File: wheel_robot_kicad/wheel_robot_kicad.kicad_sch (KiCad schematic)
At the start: 7 parts, among them M1 Motor_DC, M2 Motor_DC, U1 ESP32-C6-MINI-1, U2 LM2596S-3.3, U3 BMI160, U4 DRV8833PW, U5 DRV8833PW

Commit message: added additional IMU documentation
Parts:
- removed U1: ESP32-C6-MINI-1, RF_Module:ESP32-C6-MINI-1, symbol RF_Module:ESP32-C6-MINI-1
- removed U2: LM2596S-3.3, Package_TO_SOT_SMD:TO-263-5_TabPin3, symbol Regulator_Switching:LM2596S-3.3
- removed U4, U5: DRV8833PW, Package_SO:TSSOP-16_4.4x5mm_P0.65mm, symbol Driver_Motor:DRV8833PW
- added 450mAh_3S_LiPo_BatteryPack_45C: 11.1V, symbol Device:Battery_Cell
- added D1: 1N5822, Diode_THT:D_DO-201AD_P15.24mm_Horizontal, symbol Diode:1N5822
- added L1: 68uH, symbol Device:L
- added U1: ESP32-S3-DEVKITC-1-N8R8, ESP32-S3-DEVKITC-1-N8R8:ESP32-S3-DEVKITC-1-N8R8, symbol ESP32-S3-DEVKITC-1-N8R8:ESP32-S3-DEVKITC-1-N8R8
- added U2: TB6612FNG, Package_SO:SSOP-24_5.3x8.2mm_P0.65mm, symbol Driver_Motor:TB6612FNG
- added U4: LM2596S-5, Package_TO_SOT_SMD:TO-263-5_TabPin3, symbol Regulator_Switching:LM2596S-5
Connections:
- net GND: now also 450mAh_3S_LiPo_BatteryPack_45C.2 (-), D1.2 (A), U1.J1_22 (GND3), U1.J3_1 (GND), U1.J3_10 (GPIO38), U1.J3_11 (GPIO37), U1.J3_12 (GPIO36), U1.J3_13 (GPIO35), U1.J3_14 (GPIO0), U1.J3_15 (GPIO45), U1.J3_16 (GPIO48), U1.J3_17 (GPIO47), U1.J3_18 (GPIO21), U1.J3_19 (USB_D+/GPIO20), U1.J3_2 (U0TXD/GPIO43), U1.J3_20 (USB_D-/GPIO19), U1.J3_21 (GND1), U1.J3_22 (GND2), U1.J3_3 (U0RXD/GPIO44), U1.J3_4 (GPIO1), U1.J3_5 (GPIO2), U1.J3_6 (MTMS/GPIO42), U1.J3_7 (MTDI/GPIO41), U1.J3_8 (MTDO/GPIO40), U1.J3_9 (MTCK/GPIO39), U2.10 (PGND2), U2.16 (BIN2), U2.17 (BIN1), U2.18 (GND), U2.21 (AIN1), U2.22 (AIN2), U2.3 (PGND1), U2.4 (PGND1), U2.9 (PGND2), U4.3 (GND), U4.5 (~{ON}/OFF); no longer U3.7 (GND)
- net at U3.5 (VDDIO): no longer U3.8 (VDD)
- net at M1.1 (+): now also U2.7 (BO2), U2.8 (BO2)
- net at M1.2 (-): now also U2.11 (BO1), U2.12 (BO1)
- net at M2.1 (+): now also U2.1 (AO1), U2.2 (AO1)
- net at M2.2 (-): now also U2.5 (AO2), U2.6 (AO2)
- new net: D1.1 (K), L1.1, U4.2 (OUT)
- new net: 450mAh_3S_LiPo_BatteryPack_45C.1 (+), U4.1 (VIN)
- new net: U1.J1_18 (GPIO12), U2.15 (PWMB)
- new net: U1.J1_19 (GPIO13), U2.23 (PWMA)
- new net: U1.J1_20 (GPIO14), U2.19 (STBY)
- new net: L1.2, U1.J1_21 (5V0), U2.20 (VCC), U4.4 (FB)
- new net: U2.13 (VM2), U2.14 (VM3), U2.24 (VM1)

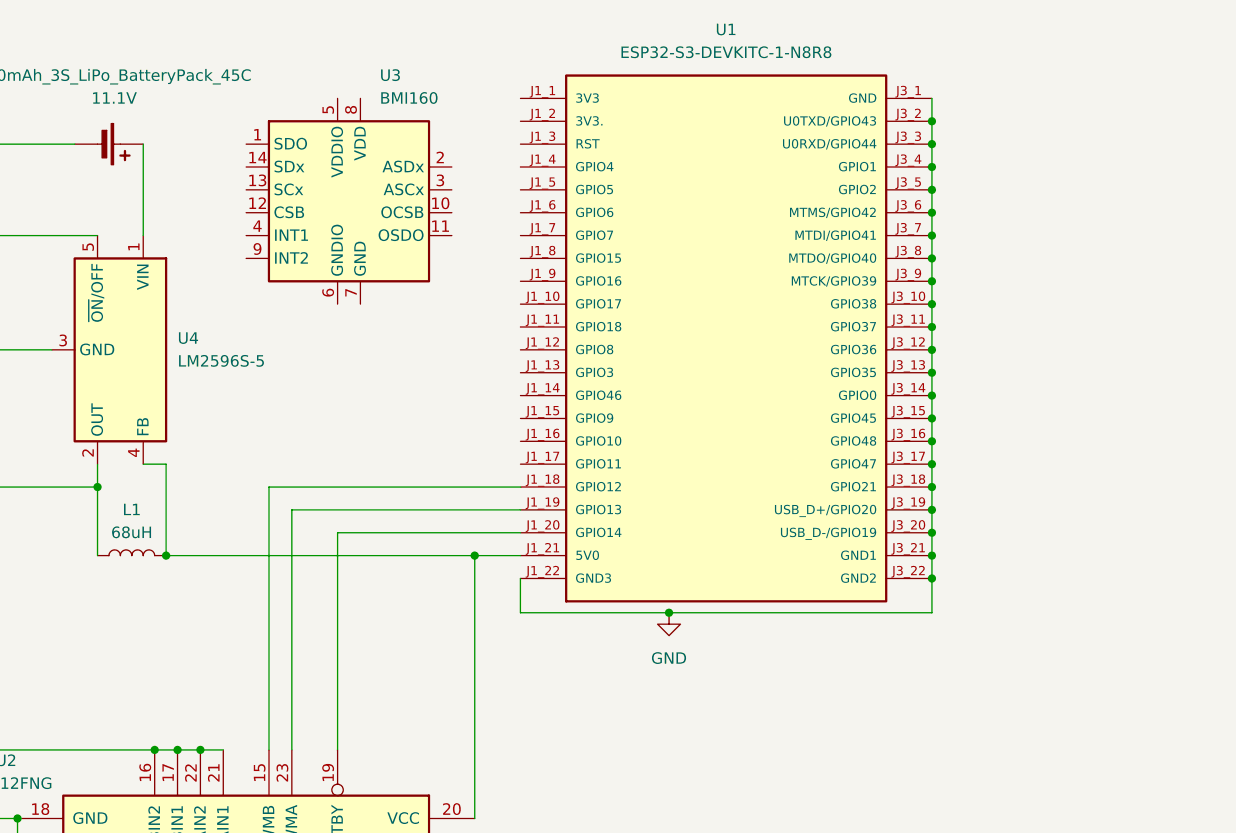
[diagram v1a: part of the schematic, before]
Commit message: updated current design to include ordered footprints
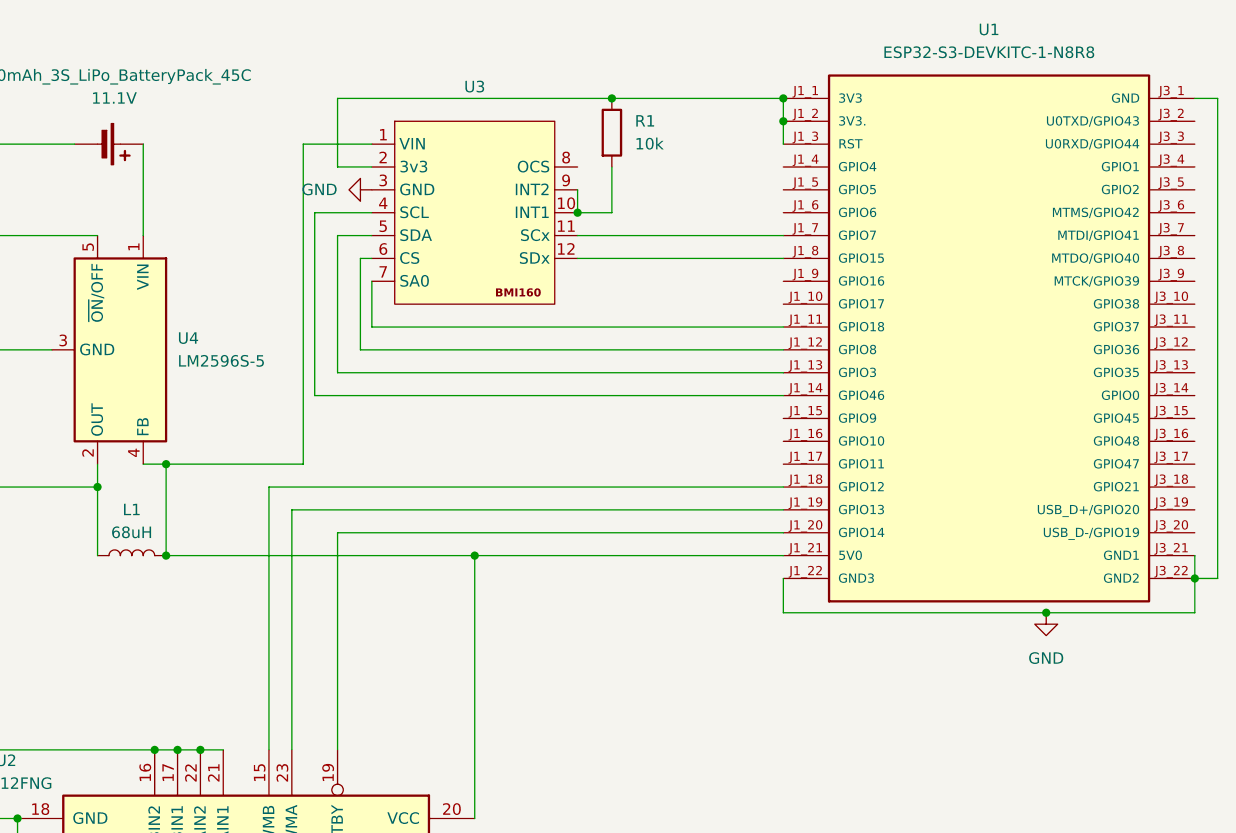
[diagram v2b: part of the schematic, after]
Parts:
- removed U3: BMI160, Package_LGA:Bosch_LGA-14_3x2.5mm_P0.5mm, symbol Sensor_Motion:BMI160
- added R1: 10k, symbol Device:R
- added U3: ~, KappyCustom:BMI160_Module_SMD, symbol KappyCustom:BMI160_Module
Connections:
- net GND: now also U3.3 (GND); no longer U1.J3_10 (GPIO38), U1.J3_11 (GPIO37), U1.J3_12 (GPIO36), U1.J3_13 (GPIO35), U1.J3_14 (GPIO0), U1.J3_15 (GPIO45), U1.J3_16 (GPIO48), U1.J3_17 (GPIO47), U1.J3_18 (GPIO21), U1.J3_19 (USB_D+/GPIO20), U1.J3_2 (U0TXD/GPIO43), U1.J3_20 (USB_D-/GPIO19), U1.J3_3 (U0RXD/GPIO44), U1.J3_4 (GPIO1), U1.J3_5 (GPIO2), U1.J3_6 (MTMS/GPIO42), U1.J3_7 (MTDI/GPIO41), U1.J3_8 (MTDO/GPIO40), U1.J3_9 (MTCK/GPIO39)
- net at U1.J1_1 (3V3): now also U1.J1_2 (3V3.), U1.J1_3 (RST), R1.1, U3.2 (3v3)
- net at U1.J1_11 (GPIO18): now also U3.7 (SA0)
- net at U1.J1_12 (GPIO8): now also U3.6 (CS)
- net at U1.J1_13 (GPIO3): now also U3.5 (SDA)
- net at U1.J1_14 (GPIO46): now also U3.4 (SCL)
- net at L1.2, U1.J1_21 (5V0), U2.20 (VCC)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: now also U3.1 (VIN)
- net at U1.J1_7 (GPIO7): now also U3.11 (SCx)
- net at U1.J1_8 (GPIO15): now also U3.12 (SDx)
- new net: R1.2, U3.10 (INT1), U3.9 (INT2)
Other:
- moved on the sheet: U1

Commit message: added motor power
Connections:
- net at 450mAh_3S_LiPo_BatteryPack_45C.1 (+), U4.1 (VIN): now also U2.13 (VM2), U2.14 (VM3), U2.24 (VM1)
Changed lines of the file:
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@@
+	)
+	(junction
+		(at 48.26 30.48)
+		(diameter 0)
+		(color 0 0 0 0)
+	)
+	(junction
+		(at 85.09 118.11)
+		(diameter 0)
+		(color 0 0 0 0)
 	)
 	(junction
@@
 	)
 	(junction
-		(at 85.09 118.11)
-		(diameter 0)
-		(color 0 0 0 0)
-	)
-	(junction
 		(at 49.53 97.79)
 		(diameter 0)
@@
 	(wire
 		(pts
+			(xy 85.09 118.11) (xy 177.8 118.11)
+		)
+		(stroke
+			(width 0)
+			(type default)
+		)
+	)
+	(wire
+		(pts
 			(xy 66.04 66.04) (xy 50.8 66.04)
 		)
@@
 	(wire
 		(pts
+			(xy 69.85 139.7) (xy 76.2 139.7)
+		)
+		(stroke
+			(width 0)
+			(type default)
+		)
+	)
+	(wire
+		(pts
+			(xy 73.66 40.64) (xy 69.85 40.64)
+		)
+		(stroke
+			(width 0)
+			(type default)
+		)
+	)
+	(wire
+		(pts
+			(xy 72.39 43.18) (xy 72.39 53.34)
+		)
+		(stroke
+			(width 0)
+			(type default)
+		)
+	)
+	(wire
+		(pts
+			(xy 43.18 68.58) (xy 43.18 76.2)
+		)
+		(stroke
+			(width 0)
+			(type default)
+		)
+	)
+	(wire
+		(pts
+			(xy 34.29 105.41) (xy 34.29 115.57)
+		)
+		(stroke
+			(width 0)
+			(type default)
+		)
+	)
+	(wire
+		(pts
+			(xy 64.77 128.27) (xy 64.77 139.7)
+		)
+		(stroke
+			(width 0)
+			(type default)
+		)
+	)
+	(wire
+		(pts
+			(xy 167.64 78.74) (xy 165.1 78.74)
+		)
+		(stroke
+			(width 0)
+			(type default)
+		)
+	)
+	(wire
+		(pts
+			(xy 60.96 139.7) (xy 60.96 149.86)
+		)
+		(stroke
+			(width 0)
+			(type default)
+		)
+	)
+	(wire
+		(pts
+			(xy 119.38 76.2) (xy 85.09 76.2)
+		)
+		(stroke
+			(width 0)
+			(type default)
+		)
+	)
+	(wire
+		(pts
+			(xy 96.52 35.56) (xy 96.52 38.1)
+		)
+		(stroke
+			(width 0)
+			(type default)
+		)
+	)
+	(wire
+		(pts
+			(xy 148.59 82.55) (xy 165.1 82.55)
+		)
+		(stroke
+			(width 0)
+			(type default)
+		)
+	)
+	(wire
+		(pts
+			(xy 50.8 66.04) (xy 48.26 66.04)
+		)
+		(stroke
+			(width 0)
+			(type default)
+		)
+	)
+	(wire
+		(pts
+			(xy 69.85 73.66) (xy 119.38 73.66)
+		)
+		(stroke
+			(width 0)
+			(type default)
+		)
+	)
+	(wire
+		(pts
 			(xy 85.09 118.11) (xy 85.09 120.65)
 		)
@@
 	(wire
 		(pts
-			(xy 69.85 139.7) (xy 76.2 139.7)
-		)
-		(stroke
-			(width 0)
-			(type default)
-		)
-	)
-	(wire
-		(pts
-			(xy 73.66 40.64) (xy 69.85 40.64)
-		)
-		(stroke
-			(width 0)
-			(type default)
-		)
-	)
-	(wire
-		(pts
-			(xy 72.39 43.18) (xy 72.39 53.34)
-		)
-		(stroke
-			(width 0)
-			(type default)
-		)
-	)
-	(wire
-		(pts
-			(xy 43.18 68.58) (xy 43.18 76.2)
-		)
-		(stroke
-			(width 0)
-			(type default)
-		)
-	)
-	(wire
-		(pts
-			(xy 34.29 105.41) (xy 34.29 115.57)
-		)
-		(stroke
-			(width 0)
-			(type default)
-		)
-	)
-	(wire
-		(pts
-			(xy 64.77 128.27) (xy 64.77 139.7)
-		)
-		(stroke
-			(width 0)
-			(type default)
-		)
-	)
-	(wire
-		(pts
-			(xy 167.64 78.74) (xy 165.1 78.74)
-		)
-		(stroke
-			(width 0)
-			(type default)
-		)
-	)
-	(wire
-		(pts
-			(xy 60.96 139.7) (xy 60.96 149.86)
-		)
-		(stroke
-			(width 0)
-			(type default)
-		)
-	)
-	(wire
-		(pts
-			(xy 119.38 76.2) (xy 85.09 76.2)
-		)
-		(stroke
-			(width 0)
-			(type default)
-		)
-	)
-	(wire
-		(pts
-			(xy 96.52 35.56) (xy 96.52 38.1)
-		)
-		(stroke
-			(width 0)
-			(type default)
-		)
-	)
-	(wire
-		(pts
-			(xy 148.59 82.55) (xy 165.1 82.55)
-		)
-		(stroke
-			(width 0)
-			(type default)
-		)
-	)
-	(wire
-		(pts
-			(xy 50.8 66.04) (xy 48.26 66.04)
-		)
-		(stroke
-			(width 0)
-			(type default)
-		)
-	)
-	(wire
-		(pts
-			(xy 69.85 73.66) (xy 119.38 73.66)
-		)
-		(stroke
-			(width 0)
-			(type default)
-		)
-	)
-	(wire
-		(pts
 			(xy 165.1 78.74) (xy 165.1 76.2)
 		)
@@
 	(wire
 		(pts
+			(xy 177.8 13.97) (xy 64.77 13.97)
+		)
+		(stroke
+			(width 0)
+			(type default)
+		)
+	)
+	(wire
+		(pts
 			(xy 21.59 30.48) (xy 21.59 40.64)
 		)
@@
 	(wire
 		(pts
+			(xy 177.8 118.11) (xy 177.8 13.97)
+		)
+		(stroke
+			(width 0)
+			(type default)
+		)
+	)
+	(wire
+		(pts
 			(xy 66.04 30.48) (xy 66.04 66.04)
 		)
@@
 	(wire
 		(pts
+			(xy 85.09 115.57) (xy 85.09 118.11)
+		)
+		(stroke
+			(width 0)
+			(type default)
+		)
+	)
+	(wire
+		(pts
 			(xy 69.85 97.79) (xy 69.85 73.66)
 		)
@@
 	(wire
 		(pts
+			(xy 64.77 13.97) (xy 64.77 30.48)
+		)
+		(stroke
+			(width 0)
+			(type default)
+		)
+	)
+	(wire
+		(pts
 			(xy 52.07 97.79) (xy 49.53 97.79)
 		)
@@
 	(wire
 		(pts
+			(xy 64.77 30.48) (xy 48.26 30.48)
+		)
+		(stroke
+			(width 0)
+			(type default)
+		)
+	)
+	(wire
+		(pts
 			(xy 34.29 115.57) (xy 34.29 120.65)
 		)
@@
 		)
 		(stroke
-			(width 0)
-			(type default)
-		)
-	)
-	(wire
-		(pts
-			(xy 85.09 115.57) (xy 85.09 118.11)
-		)
-		(stroke

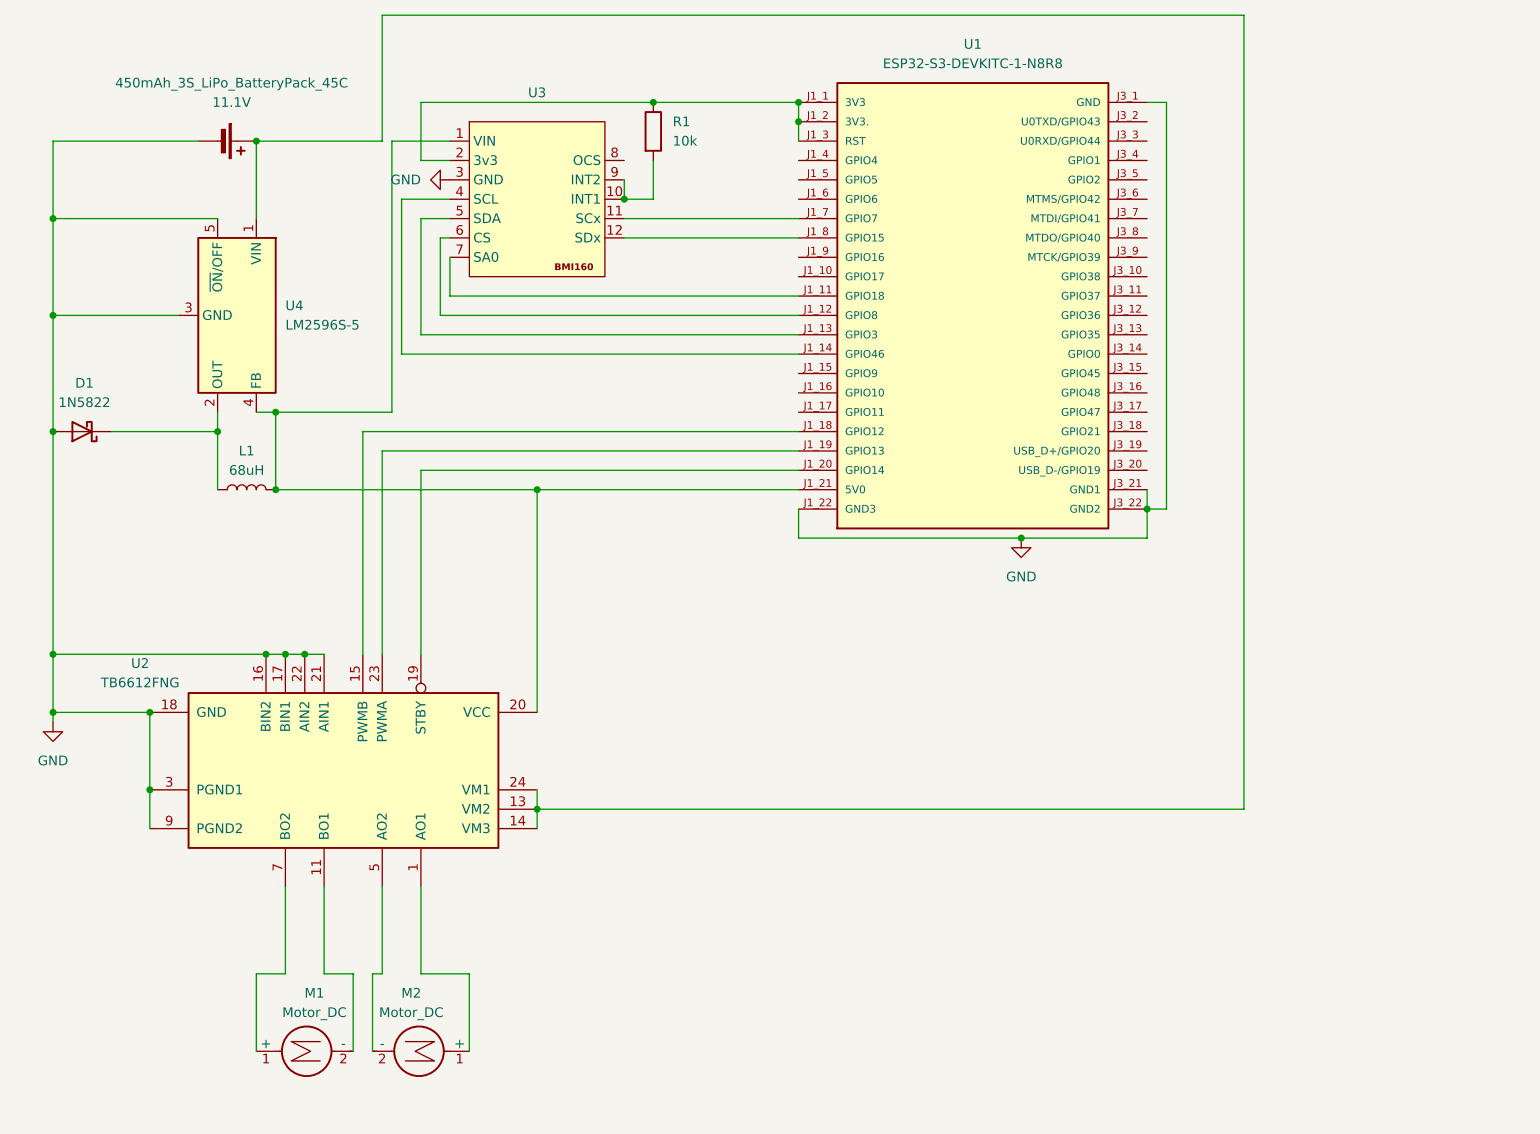
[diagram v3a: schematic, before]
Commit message: updated the curcuit to the current assembly state
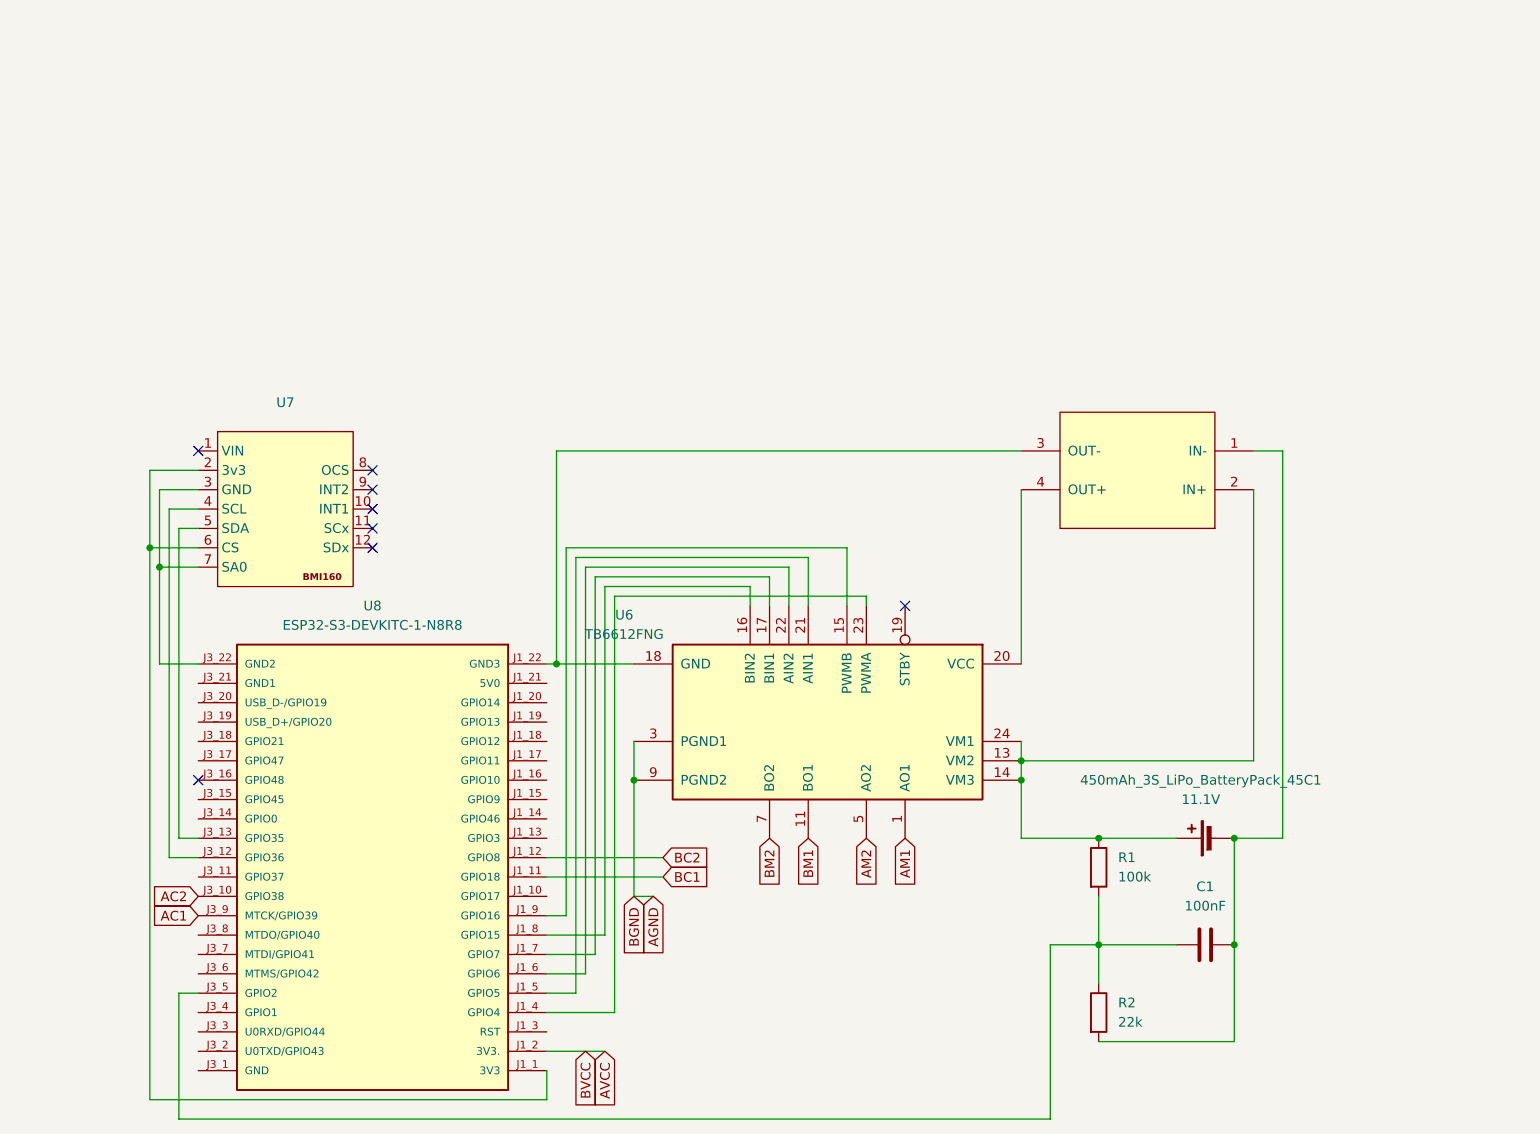
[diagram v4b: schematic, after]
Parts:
- removed 450mAh_3S_LiPo_BatteryPack_45C: 11.1V, symbol Device:Battery_Cell
- removed D1: 1N5822, Diode_THT:D_DO-201AD_P15.24mm_Horizontal, symbol Diode:1N5822
- removed L1: 68uH, symbol Device:L
- removed M1, M2: Motor_DC, symbol Motor:Motor_DC
- removed U1: ESP32-S3-DEVKITC-1-N8R8, ESP32-S3-DEVKITC-1-N8R8:ESP32-S3-DEVKITC-1-N8R8, symbol ESP32-S3-DEVKITC-1-N8R8:ESP32-S3-DEVKITC-1-N8R8
- removed U2: TB6612FNG, Package_SO:SSOP-24_5.3x8.2mm_P0.65mm, symbol Driver_Motor:TB6612FNG
- removed U3: ~, KappyCustom:BMI160_Module_SMD, symbol KappyCustom:BMI160_Module
- removed U4: LM2596S-5, Package_TO_SOT_SMD:TO-263-5_TabPin3, symbol Regulator_Switching:LM2596S-5
- added 450mAh_3S_LiPo_BatteryPack_45C1: 11.1V, symbol Device:Battery_Cell
- added C1: 100nF, symbol Device:C
- added R2: 22k, symbol Device:R
- added U4: Mini360, symbol mini360:Mini360
- added U6: TB6612FNG, Package_SO:SSOP-24_5.3x8.2mm_P0.65mm, symbol Driver_Motor:TB6612FNG
- added U7: ~, KappyCustom:BMI160_Module_SMD, symbol KappyCustom:BMI160_Module
- added U8: ESP32-S3-DEVKITC-1-N8R8, ESP32-S3-DEVKITC-1-N8R8:ESP32-S3-DEVKITC-1-N8R8, symbol ESP32-S3-DEVKITC-1-N8R8:ESP32-S3-DEVKITC-1-N8R8
- R1: value 10k -> 100k
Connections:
- net at R1.2: now also C1.1, R2.1, U8.J3_5 (GPIO2)
- net at R1.1: now also 450mAh_3S_LiPo_BatteryPack_45C1.1 (+), U4.2 (IN+), U6.13 (VM2), U6.14 (VM3), U6.24 (VM1)
- new net: 450mAh_3S_LiPo_BatteryPack_45C1.2 (-), C1.2, R2.2, U4.1 (IN-)
- new net: U4.3 (OUT-), U6.18 (GND), U8.J1_22 (GND3)
- new net: U4.4 (OUT+), U6.20 (VCC)
- new net: U6.15 (PWMB), U8.J1_9 (GPIO16)
- new net: U6.16 (BIN2), U8.J1_8 (GPIO15)
- new net: U6.17 (BIN1), U8.J1_7 (GPIO7)
- new net: U6.21 (AIN1), U8.J1_5 (GPIO5)
- new net: U6.22 (AIN2), U8.J1_6 (GPIO6)
- new net: U6.23 (PWMA), U8.J1_4 (GPIO4)
- new net: U7.2 (3v3), U7.6 (CS), U8.J1_1 (3V3)
- new net: U7.3 (GND), U7.7 (SA0), U8.J3_22 (GND2)
- new net: U7.4 (SCL), U8.J3_12 (GPIO36)
- new net: U7.5 (SDA), U8.J3_13 (GPIO35)
- new net AC1: U8.J3_9 (MTCK/GPIO39)
- new net AC2: U8.J3_10 (GPIO38)
- new net AGND: U6.10 (PGND2), U6.3 (PGND1), U6.4 (PGND1), U6.9 (PGND2)
- new net AM1: U6.1 (AO1), U6.2 (AO1)
- new net AM2: U6.5 (AO2), U6.6 (AO2)
- new net AVCC: U8.J1_2 (3V3.)
- new net BC1: U8.J1_11 (GPIO18)
- new net BC2: U8.J1_12 (GPIO8)
- new net BM1: U6.11 (BO1), U6.12 (BO1)
- new net BM2: U6.7 (BO2), U6.8 (BO2)
- no-connect marks 0 -> 8
